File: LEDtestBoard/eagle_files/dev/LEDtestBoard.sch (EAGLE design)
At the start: 18 parts, among them SW1 PCM12SMTR, SW2 PCM12SMTR, SW3 PCM12SMTR, SW4 PCM12SMTR, SW5 PCM12SMTR, SW6 PCM12SMTR, SW7 PCM12SMTR, SW8 PCM12SMTR

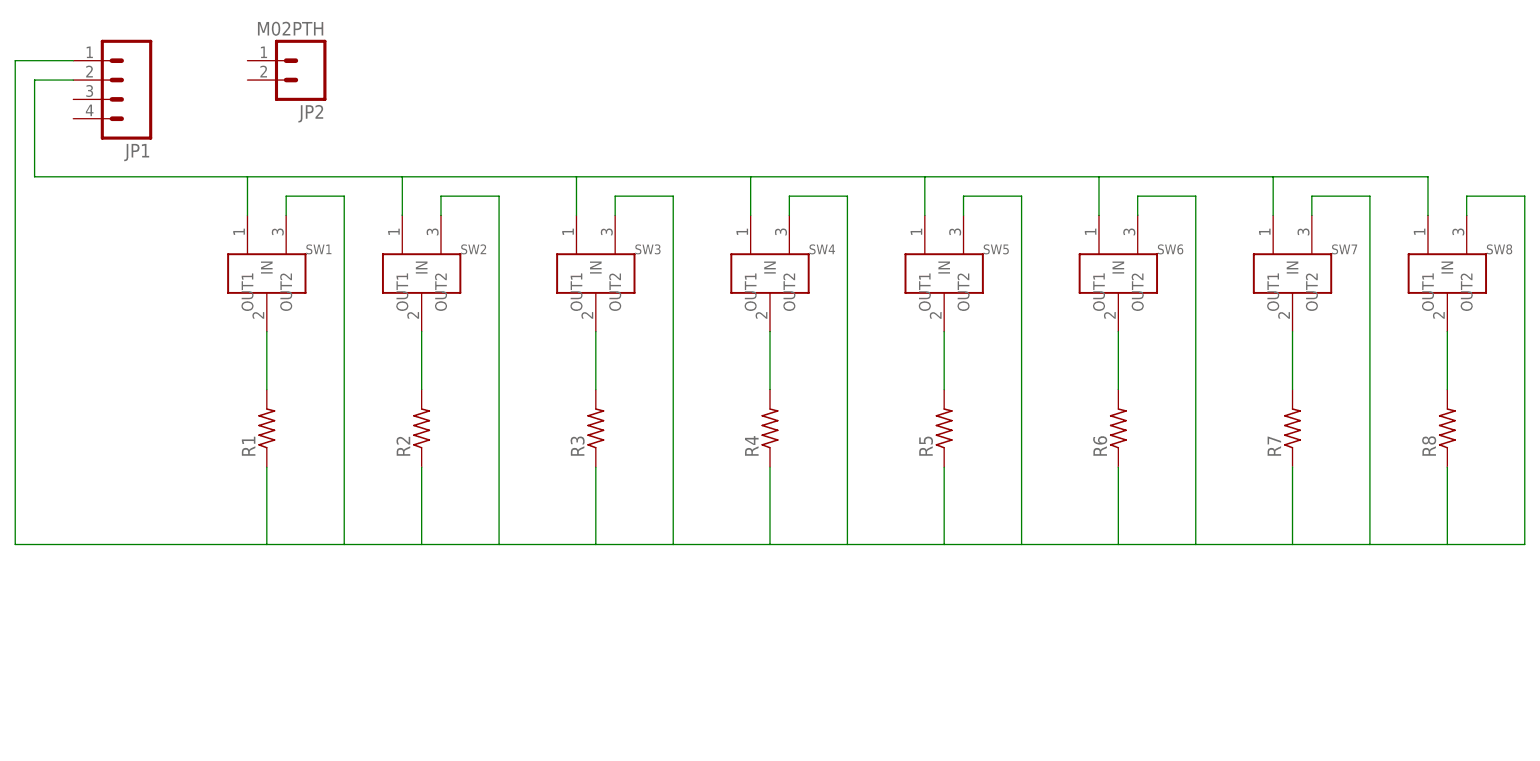
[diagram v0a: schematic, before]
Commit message: Updated LEDtestBoard dev files. Ready to begin pad check and routing.
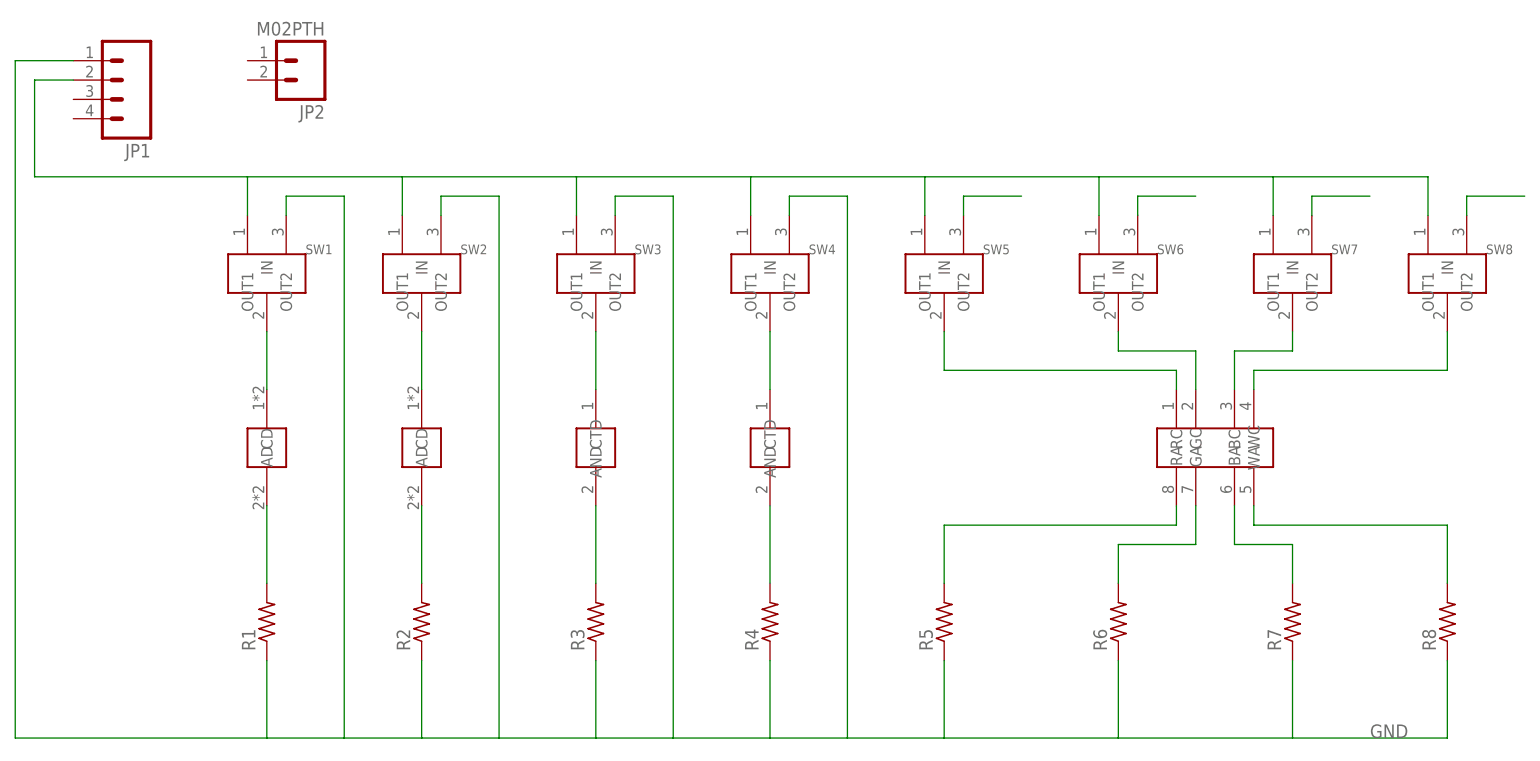
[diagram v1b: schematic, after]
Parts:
- added D1, D2: SZA05A0A, freddyLibr:SZA05A0A
- added D3: XLAMP_COLOR, freddyLibr:XLAMP_COLOR
- added D4, D5: LACN5MFBGB241Z, freddyLibr:LACN5MFBGB241Z
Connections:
- net N$6 renamed GND
- new net N$13: D3.RA, SW5.IN
- new net N$14: D3.GA, SW6.IN
- new net N$15: D3.BA, SW7.IN
- new net N$16: D3.WA, SW8.IN
- new net N$17: D3.RC, R5.2
- new net N$18: D3.GC, R6.2
- new net N$19: D3.BC, R7.2
- new net N$20: D3.WC, R8.2
- net N$10: now also D5.CTD, R4.2; no longer R8.2, SW8.IN
- net N$2: now also D1.CD; no longer SW1.IN
- net N$3: now also D1.AD, SW1.IN; no longer R2.2, SW2.IN
- net N$4: now also D2.AD, SW2.IN; no longer R3.2, SW3.IN
- net N$5: now also D2.CD, R2.2; no longer R4.2, SW4.IN
- net N$7: now also D4.CTD, R3.2; no longer R5.2, SW5.IN
- net N$8: now also D4.AND, SW3.IN; no longer R6.2, SW6.IN
- net N$9: now also D5.AND, SW4.IN; no longer R7.2, SW7.IN
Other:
- moved on the sheet: R1, R2, R3, R4, R5, R6, R7, R8

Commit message: Placed components in approximately precise locations. Ready to begin routing.
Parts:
- removed JP2: M02PTH, SparkFun-Connectors:M02PTH
- D3: value XLAMP_COLOR -> LACN5MFBGB241Z; device freddyLibr:XLAMP_COLOR -> freddyLibr:LACN5MFBGB241Z
- D5: value LACN5MFBGB241Z -> XLAMP_COLOR; device freddyLibr:LACN5MFBGB241Z -> freddyLibr:XLAMP_COLOR
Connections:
- net N$10: now also D4.CTD; no longer D5.CTD
- net N$13: now also D5.RA; no longer D3.RA
- net N$14: now also D5.GA; no longer D3.GA
- net N$15: now also D5.BA; no longer D3.BA
- net N$16: now also D5.WA; no longer D3.WA
- net N$17: now also D5.RC; no longer D3.RC
- net N$18: now also D5.GC; no longer D3.GC
- net N$19: now also D5.BC; no longer D3.BC
- net N$20: now also D5.WC; no longer D3.WC
- net N$7: now also D3.CTD; no longer D4.CTD
- net N$8: now also D3.AND; no longer D4.AND
- net N$9: now also D4.AND; no longer D5.AND
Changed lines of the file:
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@@
 <part name="R4" library="resistor" deviceset="R-US_" device="R0603"/>
 <part name="JP1" library="SparkFun-Connectors" deviceset="M04" device="PTH"/>
-<part name="JP2" library="SparkFun-Connectors" deviceset="M02" device="PTH"/>
 <part name="SW1" library="freddyLibr" deviceset="PCM12SMTR" device=""/>
 <part name="SW2" library="freddyLibr" deviceset="PCM12SMTR" device=""/>
@@
 <part name="R7" library="resistor" deviceset="R-US_" device="R0603"/>
 <part name="R8" library="resistor" deviceset="R-US_" device="R0603"/>
-<part name="D3" library="freddyLibr" deviceset="XLAMP_COLOR" device=""/>
-<part name="D4" library="freddyLibr" deviceset="LACN5MFBGB241Z" device=""/>
-<part name="D5" library="freddyLibr" deviceset="LACN5MFBGB241Z" device=""/>
 <part name="D1" library="freddyLibr" deviceset="SZA05A0A" device=""/>
 <part name="D2" library="freddyLibr" deviceset="SZA05A0A" device=""/>
+<part name="D3" library="freddyLibr" deviceset="LACN5MFBGB241Z" device=""/>
+<part name="D4" library="freddyLibr" deviceset="LACN5MFBGB241Z" device=""/>
+<part name="D5" library="freddyLibr" deviceset="XLAMP_COLOR" device=""/>
 </parts>
 <sheets>
@@
 <instance part="R4" gate="G$1" x="111.76" y="15.24" rot="R90"/>
 <instance part="JP1" gate="G$1" x="25.4" y="86.36" rot="R180"/>
-<instance part="JP2" gate="G$1" x="50.8" y="88.9" rot="R180"/>
 <instance part="SW1" gate="G$1" x="45.72" y="60.96"/>
 <instance part="SW2" gate="G$1" x="66.04" y="60.96"/>
@@
 <instance part="R7" gate="G$1" x="180.34" y="15.24" rot="R90"/>
 <instance part="R8" gate="G$1" x="200.66" y="15.24" rot="R90"/>
-<instance part="D3" gate="G$1" x="170.18" y="38.1"/>
-<instance part="D4" gate="G$1" x="88.9" y="38.1"/>
-<instance part="D5" gate="G$1" x="111.76" y="38.1"/>
 <instance part="D1" gate="G$1" x="45.72" y="38.1"/>
 <instance part="D2" gate="G$1" x="66.04" y="38.1"/>
+<instance part="D3" gate="G$1" x="88.9" y="38.1"/>
+<instance part="D4" gate="G$1" x="111.76" y="38.1"/>
+<instance part="D5" gate="G$1" x="170.18" y="38.1"/>
 </instances>
 <busses>
@@
 <pinref part="SW5" gate="G$1" pin="IN"/>
 <wire x1="134.62" y1="53.34" x2="134.62" y2="48.26" width="0.1524" layer="91"/>
-<pinref part="D3" gate="G$1" pin="RA"/>
 <wire x1="134.62" y1="48.26" x2="165.1" y2="48.26" width="0.1524" layer="91"/>
 <wire x1="165.1" y1="48.26" x2="165.1" y2="45.72" width="0.1524" layer="91"/>
+<pinref part="D5" gate="G$1" pin="RA"/>
 </segment>
 </net>
@@
 <pinref part="SW6" gate="G$1" pin="IN"/>
 <wire x1="157.48" y1="53.34" x2="157.48" y2="50.8" width="0.1524" layer="91"/>
-<pinref part="D3" gate="G$1" pin="GA"/>
 <wire x1="157.48" y1="50.8" x2="167.64" y2="50.8" width="0.1524" layer="91"/>
 <wire x1="167.64" y1="50.8" x2="167.64" y2="45.72" width="0.1524" layer="91"/>
+<pinref part="D5" gate="G$1" pin="GA"/>
 </segment>
 </net>
@@
 <pinref part="SW7" gate="G$1" pin="IN"/>
 <wire x1="180.34" y1="53.34" x2="180.34" y2="50.8" width="0.1524" layer="91"/>
-<pinref part="D3" gate="G$1" pin="BA"/>
 <wire x1="180.34" y1="50.8" x2="172.72" y2="50.8" width="0.1524" layer="91"/>
 <wire x1="172.72" y1="50.8" x2="172.72" y2="45.72" width="0.1524" layer="91"/>
+<pinref part="D5" gate="G$1" pin="BA"/>
 </segment>
 </net>
@@
 <pinref part="SW8" gate="G$1" pin="IN"/>
 <wire x1="200.66" y1="53.34" x2="200.66" y2="48.26" width="0.1524" layer="91"/>
-<pinref part="D3" gate="G$1" pin="WA"/>
 <wire x1="200.66" y1="48.26" x2="175.26" y2="48.26" width="0.1524" layer="91"/>
 <wire x1="175.26" y1="48.26" x2="175.26" y2="45.72" width="0.1524" layer="91"/>
+<pinref part="D5" gate="G$1" pin="WA"/>
 </segment>
 </net>
 <net name="N$17" class="0">
 <segment>
-<pinref part="D3" gate="G$1" pin="RC"/>
 <wire x1="165.1" y1="30.48" x2="165.1" y2="27.94" width="0.1524" layer="91"/>
 <pinref part="R5" gate="G$1" pin="2"/>
 <wire x1="165.1" y1="27.94" x2="134.62" y2="27.94" width="0.1524" layer="91"/>
 <wire x1="134.62" y1="27.94" x2="134.62" y2="20.32" width="0.1524" layer="91"/>
+<pinref part="D5" gate="G$1" pin="RC"/>
 </segment>
 </net>
 <net name="N$18" class="0">
 <segment>
-<pinref part="D3" gate="G$1" pin="GC"/>
 <wire x1="167.64" y1="30.48" x2="167.64" y2="25.4" width="0.1524" layer="91"/>
 <pinref part="R6" gate="G$1" pin="2"/>
 <wire x1="167.64" y1="25.4" x2="157.48" y2="25.4" width="0.1524" layer="91"/>
 <wire x1="157.48" y1="25.4" x2="157.48" y2="20.32" width="0.1524" layer="91"/>
+<pinref part="D5" gate="G$1" pin="GC"/>
 </segment>
 </net>
 <net name="N$19" class="0">
 <segment>
-<pinref part="D3" gate="G$1" pin="BC"/>
 <wire x1="172.72" y1="30.48" x2="172.72" y2="25.4" width="0.1524" layer="91"/>
 <pinref part="R7" gate="G$1" pin="2"/>
 <wire x1="172.72" y1="25.4" x2="180.34" y2="25.4" width="0.1524" layer="91"/>
 <wire x1="180.34" y1="25.4" x2="180.34" y2="20.32" width="0.1524" layer="91"/>
+<pinref part="D5" gate="G$1" pin="BC"/>
 </segment>
 </net>
 <net name="N$20" class="0">
 <segment>
-<pinref part="D3" gate="G$1" pin="WC"/>
 <wire x1="175.26" y1="30.48" x2="175.26" y2="27.94" width="0.1524" layer="91"/>
 <pinref part="R8" gate="G$1" pin="2"/>
 <wire x1="175.26" y1="27.94" x2="200.66" y2="27.94" width="0.1524" layer="91"/>
 <wire x1="200.66" y1="27.94" x2="200.66" y2="20.32" width="0.1524" layer="91"/>
+<pinref part="D5" gate="G$1" pin="WC"/>
 </segment>
 </net>
@@
 <segment>
 <pinref part="R1" gate="G$1" pin="2"/>
+<wire x1="45.72" y1="20.32" x2="45.72" y2="30.48" width="0.1524" layer="91"/>
 <pinref part="D1" gate="G$1" pin="CD"/>
-<wire x1="45.72" y1="20.32" x2="45.72" y2="30.48" width="0.1524" layer="91"/>
 </segment>
 </net>
 <net name="N$3" class="0">
 <segment>
-<pinref part="D1" gate="G$1" pin="AD"/>
 <pinref part="SW1" gate="G$1" pin="IN"/>
 <wire x1="45.72" y1="45.72" x2="45.72" y2="53.34" width="0.1524" layer="91"/>
+<pinref part="D1" gate="G$1" pin="AD"/>
 </segment>
 </net>
@@
 <segment>
 <pinref part="SW2" gate="G$1" pin="IN"/>
+<wire x1="66.04" y1="53.34" x2="66.04" y2="45.72" width="0.1524" layer="91"/>
 <pinref part="D2" gate="G$1" pin="AD"/>
-<wire x1="66.04" y1="53.34" x2="66.04" y2="45.72" width="0.1524" layer="91"/>
 </segment>
 </net>
 <net name="N$5" class="0">
 <segment>
-<pinref part="D2" gate="G$1" pin="CD"/>
 <pinref part="R2" gate="G$1" pin="2"/>
 <wire x1="66.04" y1="30.48" x2="66.04" y2="20.32" width="0.1524" layer="91"/>
+<pinref part="D2" gate="G$1" pin="CD"/>
 </segment>
 </net>
@@
 <segment>
 <pinref part="R3" gate="G$1" pin="2"/>
-<pinref part="D4" gate="G$1" pin="CTD"/>
 <wire x1="88.9" y1="20.32" x2="88.9" y2="30.48" width="0.1524" layer="91"/>
+<pinref part="D3" gate="G$1" pin="CTD"/>
 </segment>
 </net>
 <net name="N$8" class="0">
 <segment>
-<pinref part="D4" gate="G$1" pin="AND"/>
 <pinref part="SW3" gate="G$1" pin="IN"/>
 <wire x1="88.9" y1="45.72" x2="88.9" y2="53.34" width="0.1524" layer="91"/>
+<pinref part="D3" gate="G$1" pin="AND"/>
 </segment>
 </net>
@@
 <segment>
 <pinref part="SW4" gate="G$1" pin="IN"/>
-<pinref part="D5" gate="G$1" pin="AND"/>
 <wire x1="111.76" y1="53.34" x2="111.76" y2="45.72" width="0.1524" layer="91"/>
+<pinref part="D4" gate="G$1" pin="AND"/>
 </segment>
 </net>
 <net name="N$10" class="0">
 <segment>
-<pinref part="D5" gate="G$1" pin="CTD"/>
 <pinref part="R4" gate="G$1" pin="2"/>
 <wire x1="111.76" y1="30.48" x2="111.76" y2="20.32" width="0.1524" layer="91"/>
-</segment>
-</net>
+<pinref part="D4" gate="G$1" pin="CTD"/>
+</segment>
+</net>
